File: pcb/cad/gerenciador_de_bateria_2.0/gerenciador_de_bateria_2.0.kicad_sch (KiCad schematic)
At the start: 45 parts, among them J1 Conn_01x01_Female, J2 Conn_01x01_Female, J3 Conn_01x01_Female, J4 Conn_01x01_Female, J6 Conn_01x01_Female, J7 Conn_01x01_Female, U2 USB_BQ25629

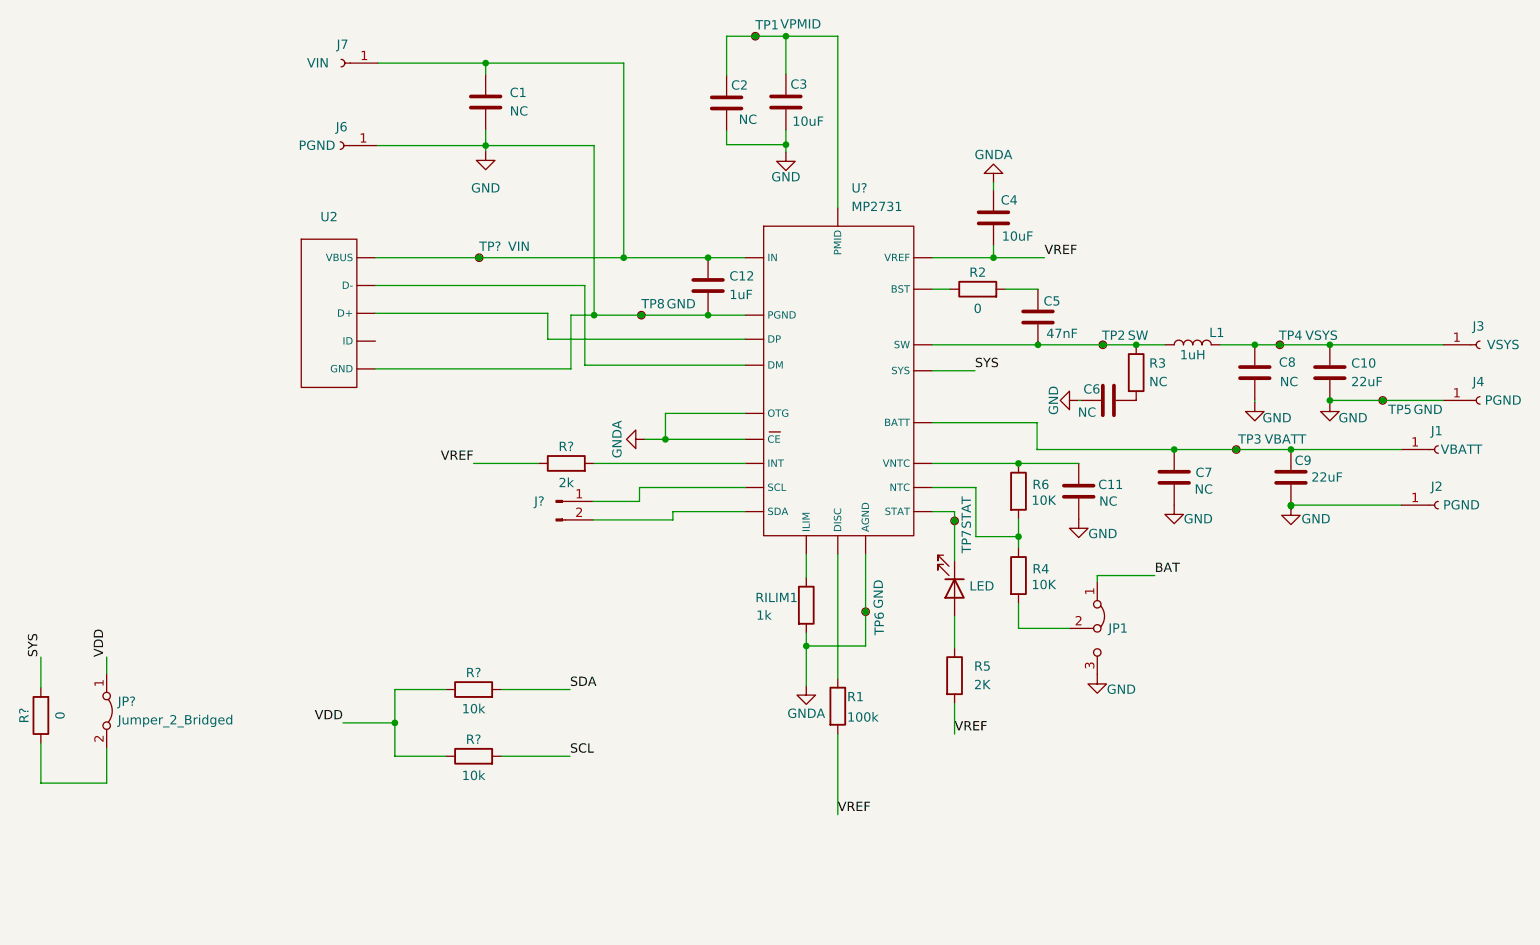
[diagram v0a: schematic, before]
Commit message: Atualização dos esquemáticos de PCB para gerenciadores de bateria
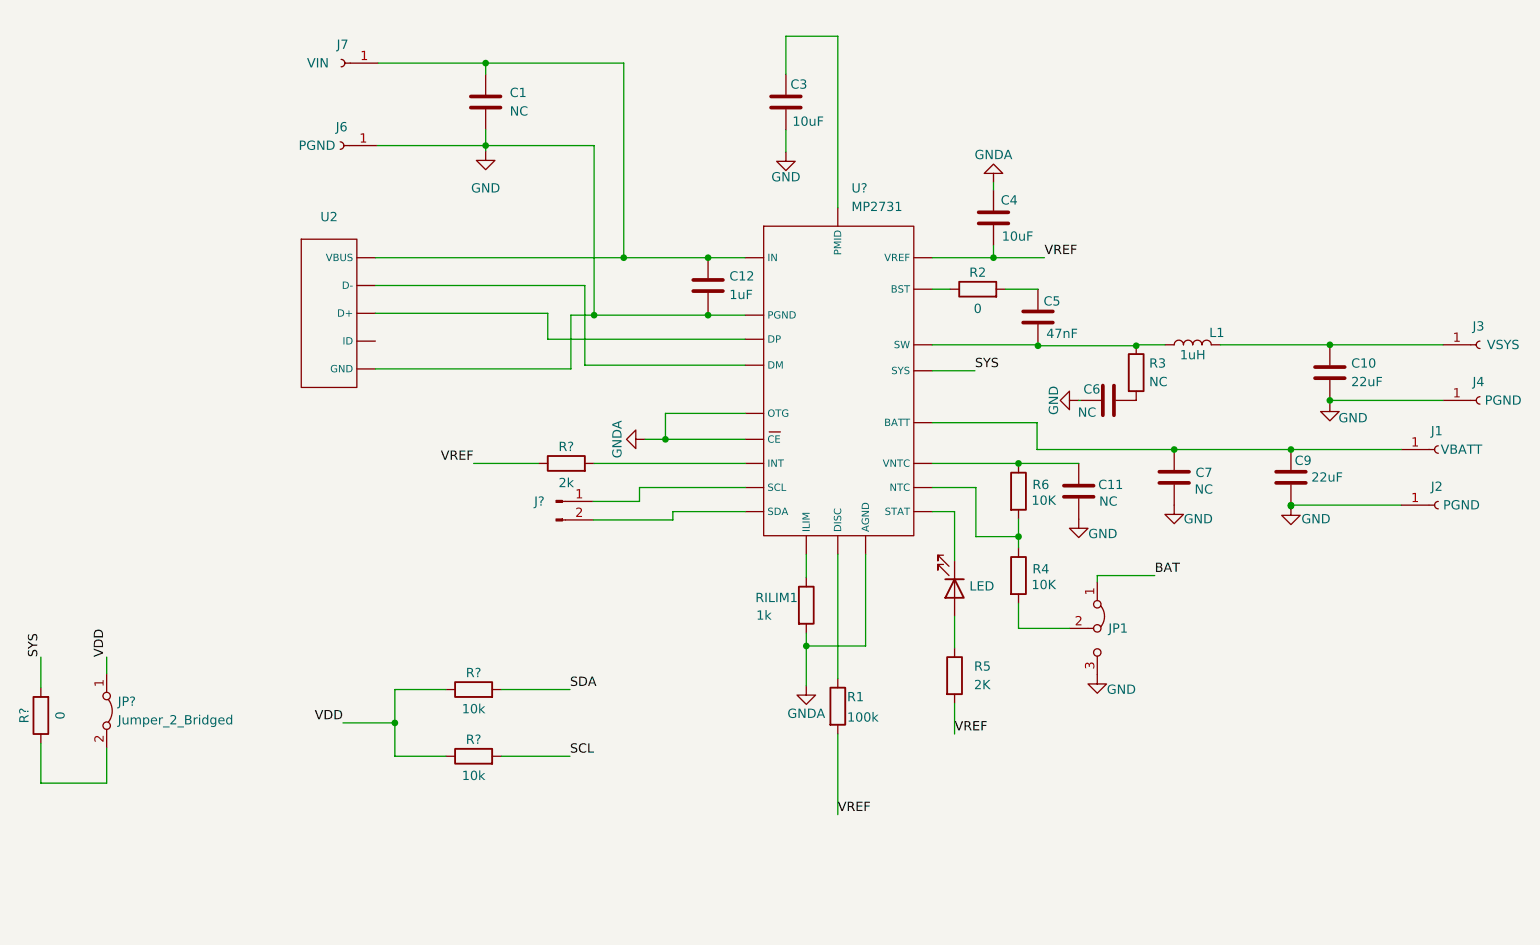
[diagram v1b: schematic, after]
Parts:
- removed C2, C8: NC, symbol Device:C
- removed TP1, TP2, TP3, TP4, TP5, TP6, TP7, TP8, TP?: TestPoint_Small, symbol Connector:TestPoint_Small
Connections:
- net at L1.1, R3.1: no longer C5.2, U?. (VREF)
- new net: C5.2, U?. (VREF)
- new net: U2. (VBUS), U?. (VREF) (x2)

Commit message: Atualização dos esquemáticos dos gerenciadores de bateria
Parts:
- removed JP1: Jumper_3_Bridged12, symbol Jumper:Jumper_3_Bridged12
- added J?: Conn_01x01_Female, symbol Connector:Conn_01x01_Female
- added R? (x2): R, symbol Device:R
- added SW1: SW_Push, symbol Switch:SW_Push
- RILIM1: value 1k -> 249
- gave numbers to parts that had none: 7
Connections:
- net GND: now also RILIM1.2; no longer C10.2, C3.2, C9.1, J2.1 (Pin_1), J4.1 (Pin_1)
- net GNDA: now also R?.2, SW1.1; no longer RILIM1.2
- net SYS: now also C10.1, J3.1 (Pin_1), L1.2
- net VREF: now also SW1.2
- net at R4.2: now also R?.1, R?.2
- new net: J?.1 (Pin_1), R?.1
- new net: U1. (VREF), U2. (VBUS) (x2)
- new net GNDPWR: C10.2, C3.2, C9.1, J2.1 (Pin_1), J4.1 (Pin_1)
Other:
- moved on the sheet: J2, J4, JP2, R7, R8, R9

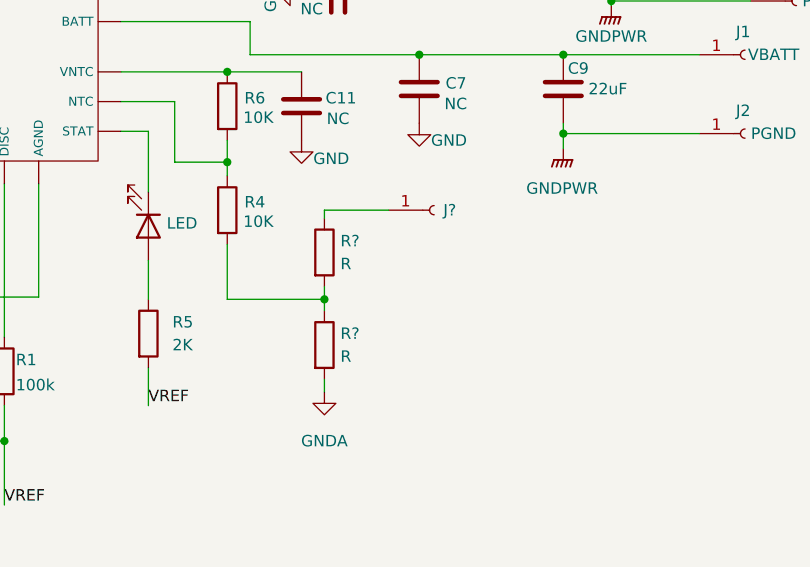
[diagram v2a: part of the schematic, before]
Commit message: Atualização nas conexões do pino NTC
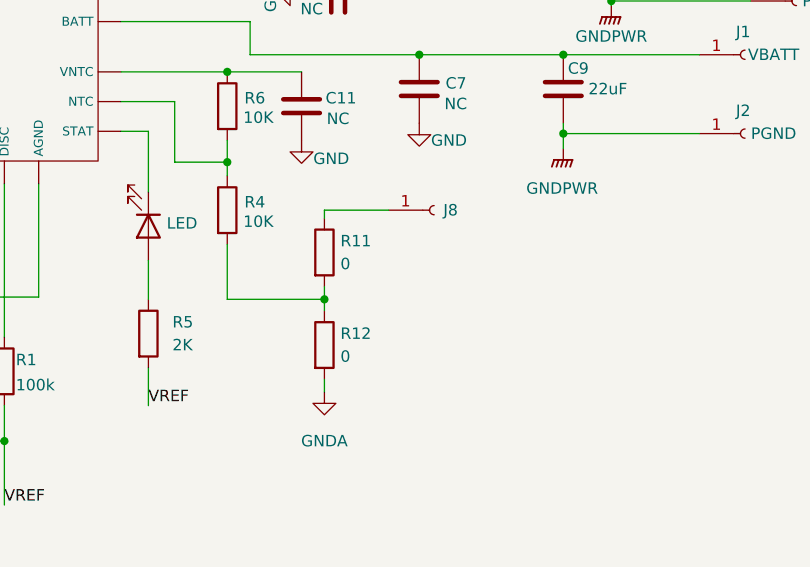
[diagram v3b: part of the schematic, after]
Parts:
- R11, R12: renamed from R?; value R -> 0
- gave numbers to parts that had none: 1
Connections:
- new net: U1. (VREF), U2. (VBUS) (x2)
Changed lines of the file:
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@@
   (symbol (lib_id "Device:R") (at 192.532 122.682 0) (unit 1)
     (in_bom yes) (on_board yes) (fields_autoplaced)
-    (property "Reference" "R?" (id 0) (at 194.31 121.4119 0)
-      (effects (font (size 1.27 1.27)) (justify left))
-    )
-    (property "Value" "R" (id 1) (at 194.31 123.9519 0)
+    (property "Reference" "R11" (id 0) (at 194.31 121.4119 0)
+      (effects (font (size 1.27 1.27)) (justify left))
+    )
+    (property "Value" "0" (id 1) (at 194.31 123.9519 0)
       (effects (font (size 1.27 1.27)) (justify left))
     )
@@
   (symbol (lib_id "Connector:Conn_01x01_Female") (at 204.724 117.983 0) (unit 1)
     (in_bom yes) (on_board yes) (fields_autoplaced)
-    (property "Reference" "J?" (id 0) (at 205.74 117.9829 0)
+    (property "Reference" "J8" (id 0) (at 205.74 117.9829 0)
       (effects (font (size 1.27 1.27)) (justify left))
     )
@@
   (symbol (lib_id "Device:R") (at 192.532 132.969 0) (unit 1)
     (in_bom yes) (on_board yes) (fields_autoplaced)
-    (property "Reference" "R?" (id 0) (at 194.31 131.6989 0)
-      (effects (font (size 1.27 1.27)) (justify left))
-    )
-    (property "Value" "R" (id 1) (at 194.31 134.2389 0)
+    (property "Reference" "R12" (id 0) (at 194.31 131.6989 0)
+      (effects (font (size 1.27 1.27)) (justify left))
+    )
+    (property "Value" "0" (id 1) (at 194.31 134.2389 0)
       (effects (font (size 1.27 1.27)) (justify left))
     )
@@
     )
     (path "/b162b72c-a401-4f88-8762-c17b000a5a94"
-      (reference "J?") (unit 1) (value "Conn_01x01_Female") (footprint "")
+      (reference "J8") (unit 1) (value "Conn_01x01_Female") (footprint "")
     )
     (path "/351e6e42-b0e7-40fb-b8ab-dd6f8578ce8a"
@@
     )
     (path "/1d4c09f2-1cd0-49ac-b0b6-730aea19e55f"
-      (reference "R?") (unit 1) (value "R") (footprint "")
+      (reference "R11") (unit 1) (value "0") (footprint "")
     )
     (path "/b92037af-d7b8-403e-b62d-15766d19f85c"
-      (reference "R?") (unit 1) (value "R") (footprint "")
+      (reference "R12") (unit 1) (value "0") (footprint "")
     )
     (path "/aa1223a0-8c51-4284-b76d-b648d59b933a"

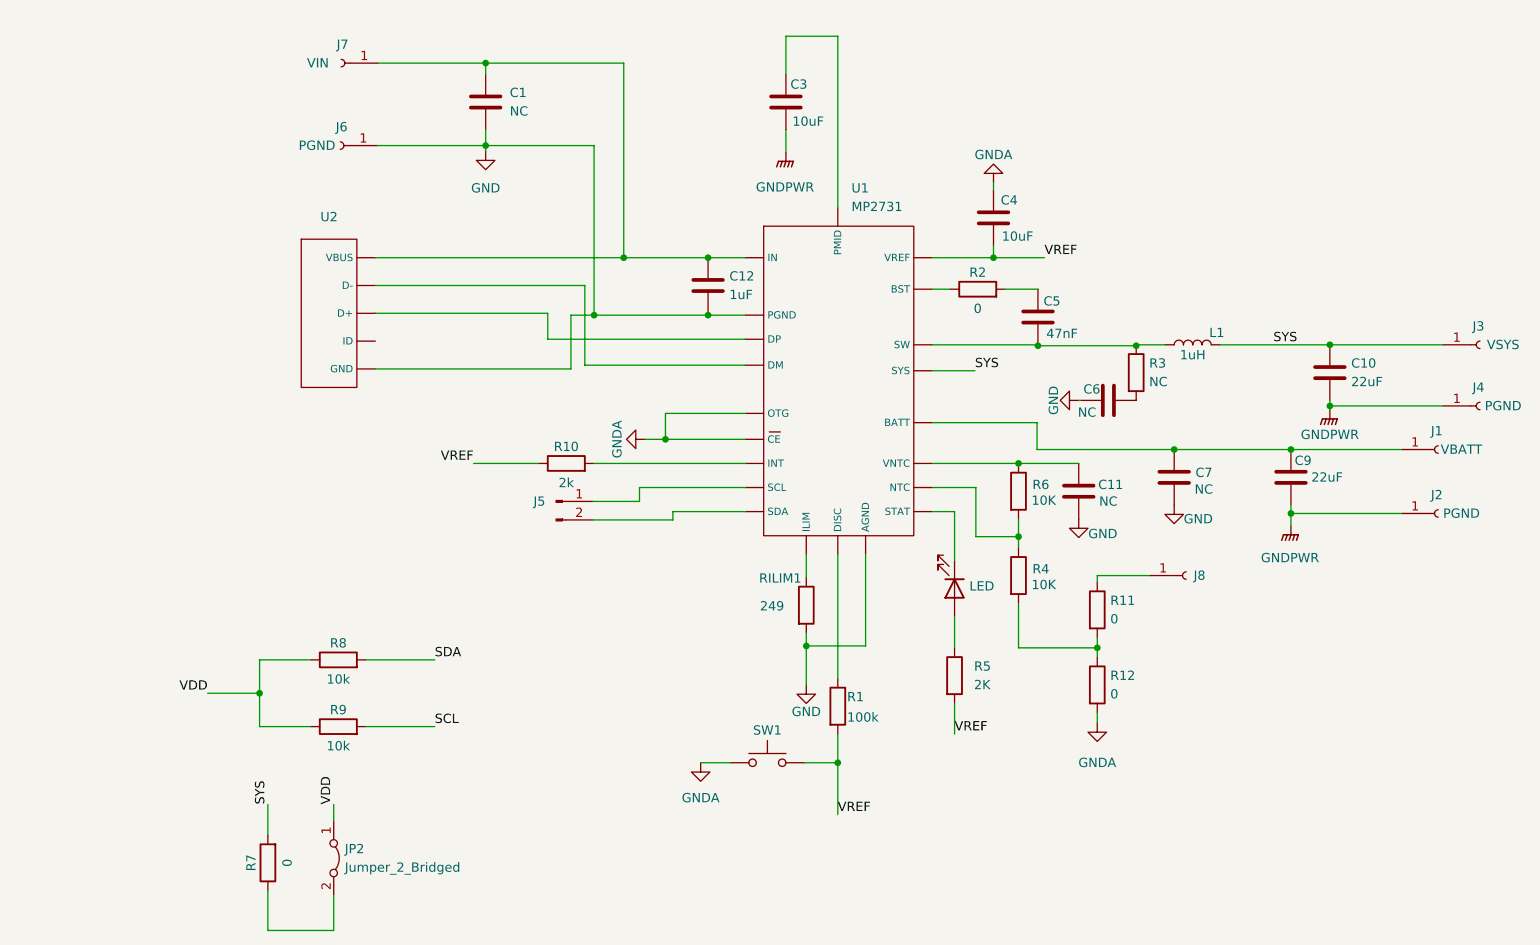
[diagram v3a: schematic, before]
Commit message: Associação dos footprint e início do layout da PCB
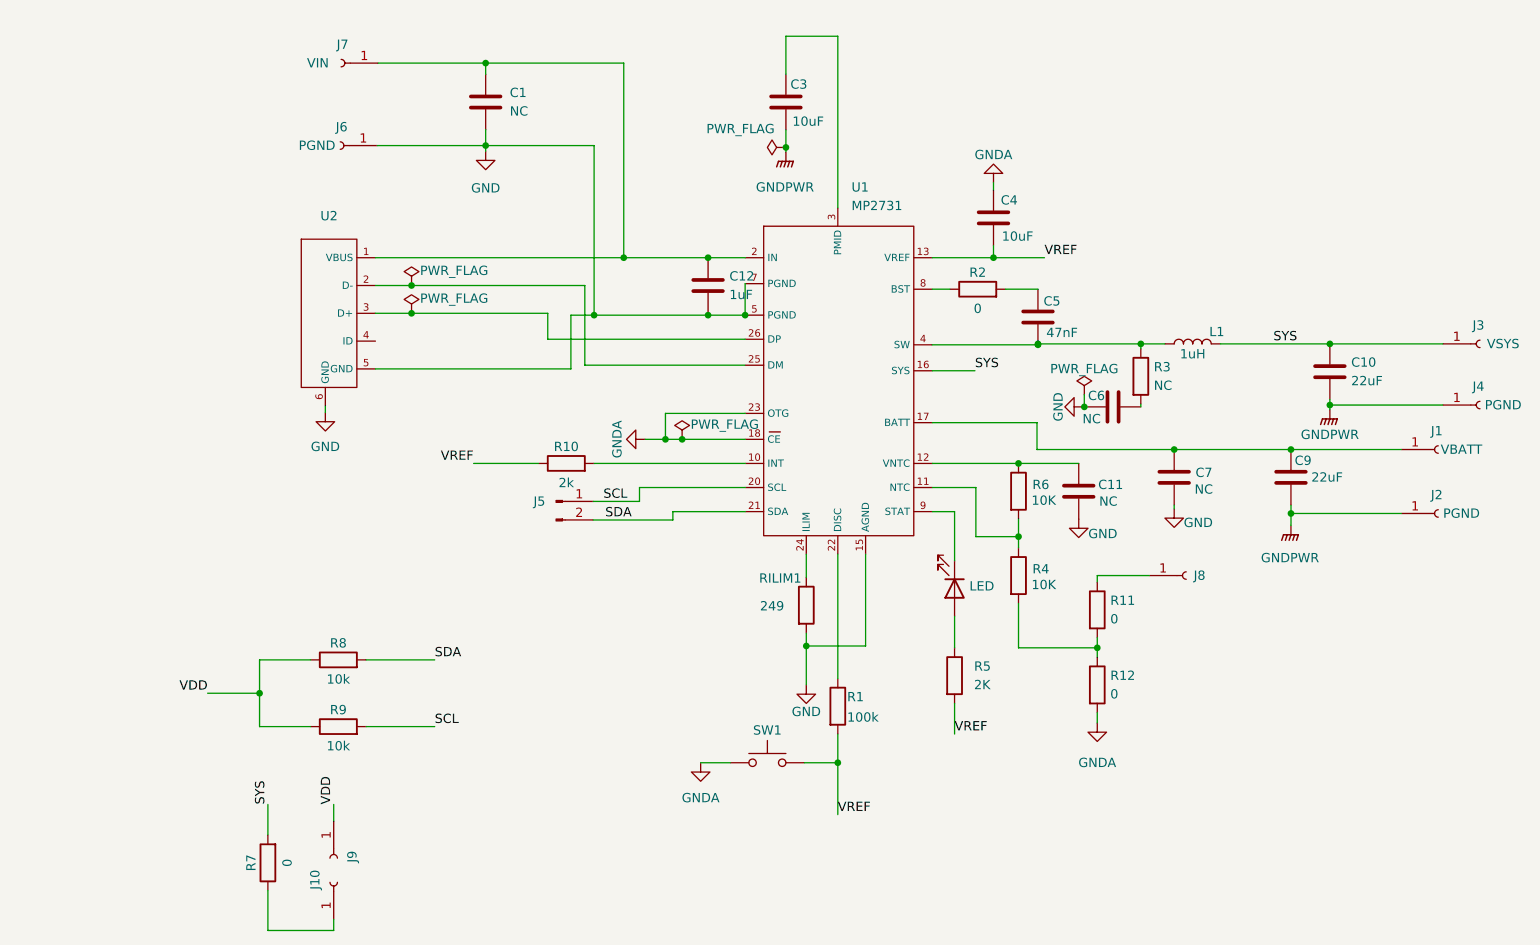
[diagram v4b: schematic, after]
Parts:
- removed JP2: Jumper_2_Bridged, symbol Jumper:Jumper_2_Bridged
- added J10, J9: Conn_01x01_Female, Connector_PinHeader_2.54mm:PinHeader_1x01_P2.54mm_Vertical, symbol Connector:Conn_01x01_Female
- C1, C10, C11, C12, C3, C4, C5, C7, C9: footprint (none) -> Capacitor_SMD:C_0805_2012Metric
- D1: footprint (none) -> LED_SMD:LED_0805_2012Metric
- J1, J2, J3, J4, J6, J7, J8: footprint (none) -> Connector_PinHeader_2.54mm:PinHeader_1x01_P2.54mm_Vertical
- J5: footprint (none) -> Connector_PinHeader_2.54mm:PinHeader_1x02_P2.54mm_Vertical
- L1: footprint (none) -> Inductor_SMD:L_0805_2012Metric
- R1, R10, R11, R12, R2, R3, R4, R5, R6, R7, R8, R9, RILIM1: footprint (none) -> Resistor_SMD:R_0805_2012Metric
- SW1: footprint (none) -> Button_Switch_THT:SW_PUSH_6mm
- U1: footprint (none) -> gerenciador_de_bateria_2:QFN-26_MP2731
- U2: footprint (none) -> Connector_USB:USB_Micro-B_Amphenol_10118194_Horizontal
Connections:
- net GND: now also U1.15 (AGND), U1.5 (PGND), U1.7 (PGND), U2.5 (GND), U2.6 (GND); no longer U1. (VREF), U2. (VBUS)
- net GNDA: now also U1.18 (CE), U1.23 (OTG); no longer U1. (VREF)
- net SCL: now also J5.1 (Pin_1), U1.20 (SCL)
- net SDA: now also J5.2 (Pin_2), U1.21 (SDA)
- net SYS: now also U1.16 (SYS); no longer U1. (VREF)
- net VDD: now also J9.1 (Pin_1)
- net VREF: now also U1.13 (VREF); no longer U1. (VREF)
- net at R2.1: now also U1.8 (BST); no longer U1. (VREF)
- net at R7.1: now also J10.1 (Pin_1)
- net at C11.2, R6.1: now also U1.12 (VNTC); no longer U1. (VREF)
- net at R4.1, R6.2: now also U1.11 (NTC); no longer U1. (VREF)
- net at C1.1, C12.1, J7.1 (Pin_1): now also U1.2 (IN), U2.1 (VBUS); no longer U1. (VREF), U2. (VBUS)
- net at R1.1: now also U1.22 (DISC); no longer U1. (VREF)
- net at C7.1, C9.2, J1.1 (Pin_1): now also U1.17 (BATT); no longer U1. (VREF)
- net at L1.1, R3.1: now also C5.2, U1.4 (SW)
- net at C3.1: now also U1.3 (PMID); no longer U1. (VREF)
- net at D1.1 (K): now also U1.9 (STAT); no longer U1. (VREF)
- net at RILIM1.1: now also U1.24 (ILIM); no longer U1. (VREF)
- net at R10.2: now also U1.10 (INT); no longer U1. (VREF)
- new net: U1.25 (DM), U2.2 (D-)
- new net: U1.26 (DP), U2.3 (D+)
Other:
- moved on the sheet: C6, R3

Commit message: Alteração no GND do esquemático para GNDA ou GNDPWR, finalização da PCB do gerenciador de bateria 2.0
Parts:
- C6: footprint (none) -> Capacitor_SMD:C_0805_2012Metric
- L1: footprint Inductor_SMD:L_0805_2012Metric -> Inductor_SMD:L_1210_3225Metric
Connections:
- net GND is gone; now on net GNDA: C1.2, C11.1, C12.2, C6.2, C7.2, J6.1 (Pin_1), RILIM1.2, U1.15 (AGND), U1.5 (PGND), U1.7 (PGND), U2.5 (GND), U2.6 (GND)
- net GNDPWR is gone; now on net GNDA: C10.2, C3.2, C9.1, J2.1 (Pin_1), J4.1 (Pin_1)
- net VREF: now also U1.14 (VREF)

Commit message: Alterações no lauout de PCB
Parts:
- removed C1: NC, Capacitor_SMD:C_0805_2012Metric, symbol Device:C
- removed J10, J9: Conn_01x01_Female, Connector_PinHeader_2.54mm:PinHeader_1x01_P2.54mm_Vertical, symbol Connector:Conn_01x01_Female
- removed R9: 10k, Resistor_SMD:R_0805_2012Metric, symbol Device:R
- J1: Campo4 VBATT -> BATT
- R7: value 0 -> 10k
- renumbered J8 to TERM1
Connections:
- net VDD is gone; now on net SYS: R8.1
- net GNDA: no longer C10.2, C12.2, C3.2, C6.2, C7.2, C9.1, J2.1 (Pin_1), J4.1 (Pin_1), J6.1 (Pin_1), U1.5 (PGND), U1.7 (PGND), U2.5 (GND), U2.6 (GND)
- net SCL: now also R7.2
- net SYS: now also R7.1; no longer R7.2
- new net GNDPWR: C10.2, C12.2, C3.2, C6.2, C7.2, C9.1, J2.1 (Pin_1), J4.1 (Pin_1), J6.1 (Pin_1), U1.5 (PGND), U1.7 (PGND), U2.5 (GND), U2.6 (GND)
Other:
- moved on the sheet: J5
